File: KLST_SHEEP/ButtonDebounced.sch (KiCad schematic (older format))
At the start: 4 parts, among them SW6 BUTTON

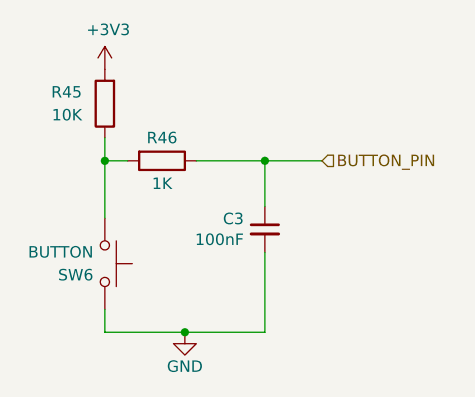
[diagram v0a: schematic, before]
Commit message: added NHD display
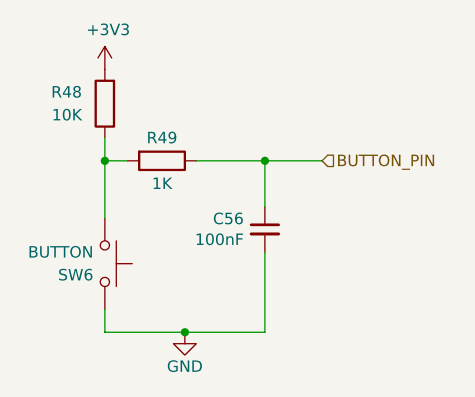
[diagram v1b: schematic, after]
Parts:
- renumbered C3 to C56, R45 to R48, R46 to R49
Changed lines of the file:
@@
 AR Path="/6075A95B/6059D173" Ref="#PWR?"  Part="1"
 AR Path="/607910C2/6059D173" Ref="#PWR?"  Part="1"
-AR Path="/6058FDA0/6059D173" Ref="#PWR074"  Part="1"
-F 0 "#PWR074" H 5850 4150 50  0001 C CNN
+AR Path="/6058FDA0/6059D173" Ref="#PWR079"  Part="1"
+F 0 "#PWR079" H 5850 4150 50  0001 C CNN
 F 1 "GND" H 5850 4250 50  0000 C CNN
 F 2 "" H 5850 4400 50  0001 C CNN
@@
 AR Path="/6075A95B/6059D1CD" Ref="R?"  Part="1"
 AR Path="/607910C2/6059D1CD" Ref="R?"  Part="1"
-AR Path="/6058FDA0/6059D1CD" Ref="R45"  Part="1"
-F 0 "R45" H 5600 3350 50  0000 L CNN
+AR Path="/6058FDA0/6059D1CD" Ref="R48"  Part="1"
+F 0 "R48" H 5600 3350 50  0000 L CNN
 F 1 "10K" H 5600 3450 50  0000 L CNN
 F 2 "Resistor_SMD:R_0402_1005Metric" V 5430 3400 50  0001 C CNN
@@
 AR Path="/6075A95B/6059D1D6" Ref="C?"  Part="1"
 AR Path="/607910C2/6059D1D6" Ref="C?"  Part="1"
-AR Path="/6058FDA0/6059D1D6" Ref="C3"  Part="1"
-F 0 "C3" H 6292 3996 50  0000 L CNN
+AR Path="/6058FDA0/6059D1D6" Ref="C56"  Part="1"
+F 0 "C56" H 6292 3996 50  0000 L CNN
 F 1 "100nF" H 6292 3905 50  0000 L CNN
 F 2 "Capacitor_SMD:C_0402_1005Metric" H 6200 3950 50  0001 C CNN
@@
 AR Path="/6075A95B/6059D1E5" Ref="R?"  Part="1"
 AR Path="/607910C2/6059D1E5" Ref="R?"  Part="1"
-AR Path="/6058FDA0/6059D1E5" Ref="R46"  Part="1"
-F 0 "R46" V 5650 3650 50  0000 C CNN
+AR Path="/6058FDA0/6059D1E5" Ref="R49"  Part="1"
+F 0 "R49" V 5650 3650 50  0000 C CNN
 F 1 "1K" V 5850 3650 50  0000 C CNN
 F 2 "Resistor_SMD:R_0402_1005Metric" V 5680 3650 50  0001 C CNN
@@
 AR Path="/6075A95B/6059D204" Ref="#PWR?"  Part="1"
 AR Path="/607910C2/6059D204" Ref="#PWR?"  Part="1"
-AR Path="/6058FDA0/6059D204" Ref="#PWR073"  Part="1"
-F 0 "#PWR073" H 5500 3100 50  0001 C CNN
+AR Path="/6058FDA0/6059D204" Ref="#PWR078"  Part="1"
+F 0 "#PWR078" H 5500 3100 50  0001 C CNN
 F 1 "+3V3" H 5515 3423 50  0000 C CNN
 F 2 "" H 5500 3250 50  0001 C CNN

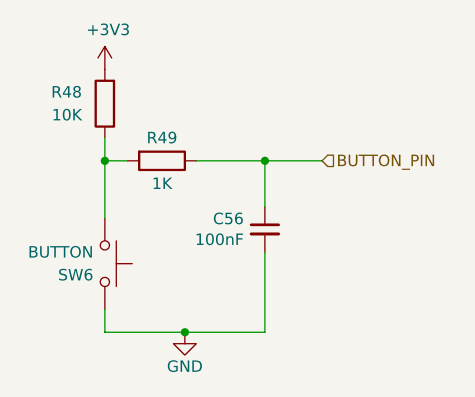
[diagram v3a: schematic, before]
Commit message: added icons
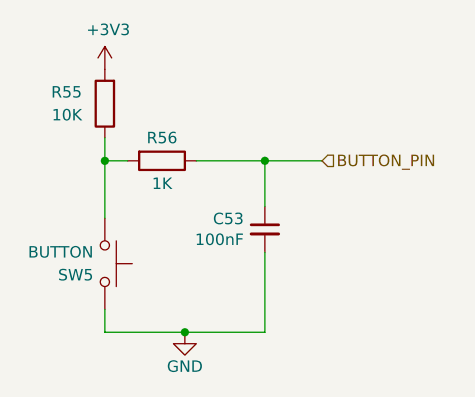
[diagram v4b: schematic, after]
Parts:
- renumbered C56 to C53, R48 to R55, R49 to R56, SW6 to SW5
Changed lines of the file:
@@
 P 5500 4100
 AR Path="/60596300" Ref="SW?"  Part="1"
-AR Path="/6058FDA0/60596300" Ref="SW6"  Part="1"
-F 0 "SW6" V 5550 4050 50  0000 R CNN
+AR Path="/6058FDA0/60596300" Ref="SW5"  Part="1"
+F 0 "SW5" V 5550 4050 50  0000 R CNN
 F 1 "BUTTON" V 5450 4050 50  0000 R CNN
 F 2 "Button_Switch_SMD:SW_Push_SPST_NO_Alps_SKRK" H 5500 4300 50  0001 C CNN
@@
 AR Path="/6075A95B/6059D173" Ref="#PWR?"  Part="1"
 AR Path="/607910C2/6059D173" Ref="#PWR?"  Part="1"
-AR Path="/6058FDA0/6059D173" Ref="#PWR079"  Part="1"
-F 0 "#PWR079" H 5850 4150 50  0001 C CNN
+AR Path="/6058FDA0/6059D173" Ref="#PWR081"  Part="1"
+F 0 "#PWR081" H 5850 4150 50  0001 C CNN
 F 1 "GND" H 5850 4250 50  0000 C CNN
 F 2 "" H 5850 4400 50  0001 C CNN
@@
 AR Path="/6075A95B/6059D1CD" Ref="R?"  Part="1"
 AR Path="/607910C2/6059D1CD" Ref="R?"  Part="1"
-AR Path="/6058FDA0/6059D1CD" Ref="R48"  Part="1"
-F 0 "R48" H 5600 3350 50  0000 L CNN
+AR Path="/6058FDA0/6059D1CD" Ref="R55"  Part="1"
+F 0 "R55" H 5600 3350 50  0000 L CNN
 F 1 "10K" H 5600 3450 50  0000 L CNN
 F 2 "Resistor_SMD:R_0402_1005Metric" V 5430 3400 50  0001 C CNN
@@
 AR Path="/6075A95B/6059D1D6" Ref="C?"  Part="1"
 AR Path="/607910C2/6059D1D6" Ref="C?"  Part="1"
-AR Path="/6058FDA0/6059D1D6" Ref="C56"  Part="1"
-F 0 "C56" H 6292 3996 50  0000 L CNN
+AR Path="/6058FDA0/6059D1D6" Ref="C53"  Part="1"
+F 0 "C53" H 6292 3996 50  0000 L CNN
 F 1 "100nF" H 6292 3905 50  0000 L CNN
 F 2 "Capacitor_SMD:C_0402_1005Metric" H 6200 3950 50  0001 C CNN
@@
 AR Path="/6075A95B/6059D1E5" Ref="R?"  Part="1"
 AR Path="/607910C2/6059D1E5" Ref="R?"  Part="1"
-AR Path="/6058FDA0/6059D1E5" Ref="R49"  Part="1"
-F 0 "R49" V 5650 3650 50  0000 C CNN
+AR Path="/6058FDA0/6059D1E5" Ref="R56"  Part="1"
+F 0 "R56" V 5650 3650 50  0000 C CNN
 F 1 "1K" V 5850 3650 50  0000 C CNN
 F 2 "Resistor_SMD:R_0402_1005Metric" V 5680 3650 50  0001 C CNN
@@
 AR Path="/6075A95B/6059D204" Ref="#PWR?"  Part="1"
 AR Path="/607910C2/6059D204" Ref="#PWR?"  Part="1"
-AR Path="/6058FDA0/6059D204" Ref="#PWR078"  Part="1"
-F 0 "#PWR078" H 5500 3100 50  0001 C CNN
+AR Path="/6058FDA0/6059D204" Ref="#PWR080"  Part="1"
+F 0 "#PWR080" H 5500 3100 50  0001 C CNN
 F 1 "+3V3" H 5515 3423 50  0000 C CNN
 F 2 "" H 5500 3250 50  0001 C CNN

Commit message: KLST_SHEEP-v0.1
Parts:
- C53: JLCPCB Part # (none) -> C1525; LCSC Part # C1525 -> (none)
- R55: JLCPCB Part # (none) -> C25744; LCSC Part # C25744 -> (none)
- R56: JLCPCB Part # (none) -> C11702; LCSC Part # C11702 -> (none)
- SW5: JLCPCB Part # (none) -> C115357; LCSC Part # C115357 -> (none)
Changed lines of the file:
@@
 F 3 "~" H 5500 4300 50  0001 C CNN
 F 4 "SKRKAEE020" V 5500 4100 50  0001 C CNN "MFR.Part #"
-F 5 "C115357" V 5500 4100 50  0001 C CNN "LCSC Part #"
+F 5 "" V 5500 4100 50  0001 C CNN "LCSC Part #"
 F 6 "x" H 5500 4100 50  0001 C CNN "Extended Part"
+F 7 "C115357" H 5500 4100 50  0001 C CNN "JLCPCB Part #"
 	1    5500 4100
 	0    1    1    0
@@
 F 3 "~" H 5500 3400 50  0001 C CNN
 F 4 "0402WGF1002TCE" H 5500 3400 50  0001 C CNN "MFR.Part #"
-F 5 "C25744" H 5500 3400 50  0001 C CNN "LCSC Part #"
+F 5 "" H 5500 3400 50  0001 C CNN "LCSC Part #"
 F 6 "-" H 5500 3400 50  0001 C CNN "Extended Part"
+F 7 "C25744" H 5500 3400 50  0001 C CNN "JLCPCB Part #"
 	1    5500 3400
 	-1   0    0    1
@@
 F 3 "~" H 6200 3950 50  0001 C CNN
 F 4 "CL05B104KO5NNNC" H 6200 3950 50  0001 C CNN "MFR.Part #"
-F 5 "C1525" H 6200 3950 50  0001 C CNN "LCSC Part #"
+F 5 "" H 6200 3950 50  0001 C CNN "LCSC Part #"
 F 6 "-" H 6200 3950 50  0001 C CNN "Extended Part"
+F 7 "C1525" H 6200 3950 50  0001 C CNN "JLCPCB Part #"
 	1    6200 3950
 	-1   0    0    -1
@@
 F 3 "~" H 5750 3650 50  0001 C CNN
 F 4 "0402WGF1001TCE" V 5750 3650 50  0001 C CNN "MFR.Part #"
-F 5 "C11702" H 5750 3650 50  0001 C CNN "LCSC Part #"
+F 5 "" H 5750 3650 50  0001 C CNN "LCSC Part #"
 F 6 "-" H 5750 3650 50  0001 C CNN "Extended Part"
+F 7 "C11702" H 5750 3650 50  0001 C CNN "JLCPCB Part #"
 	1    5750 3650
 	0    1    1    0
